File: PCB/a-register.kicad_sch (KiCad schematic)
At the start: 12 parts

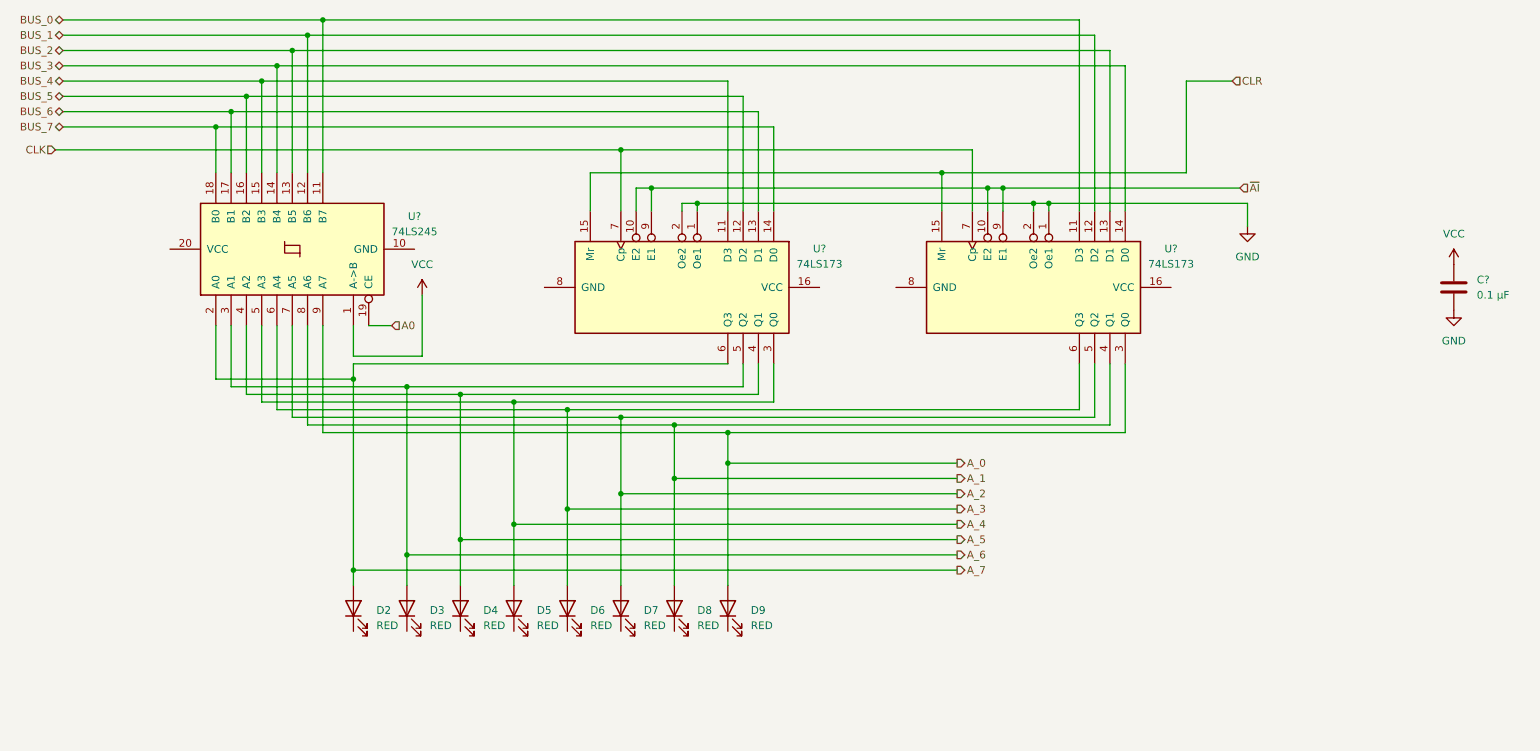
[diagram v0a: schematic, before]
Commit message: Cleaned up the schematic and got started on assigning all the footprints to the symbols
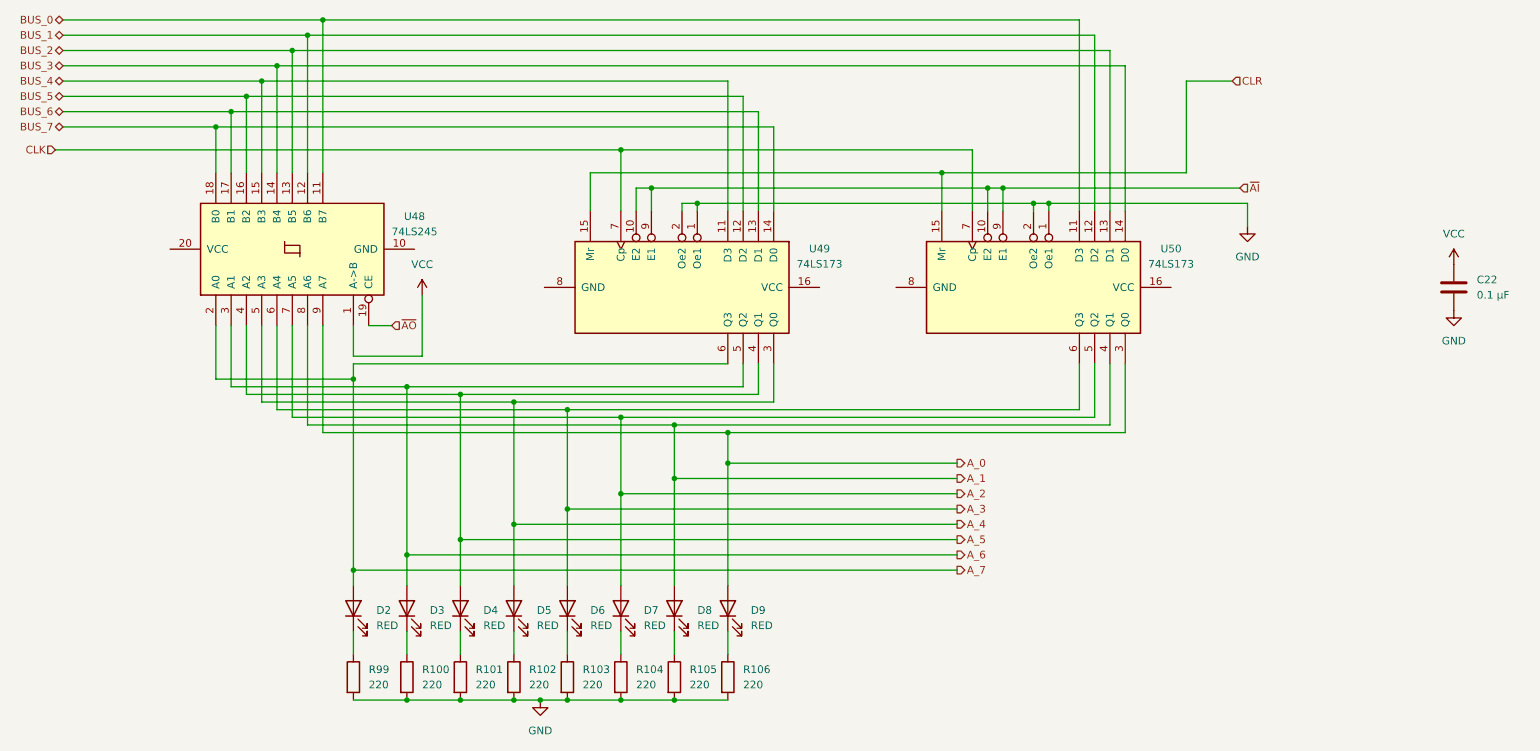
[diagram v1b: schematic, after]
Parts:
- added R100, R101, R102, R103, R104, R105, R106, R99: 220, Resistor_THT:R_Axial_DIN0207_L6.3mm_D2.5mm_P7.62mm_Horizontal, symbol Device:R
- C22: renamed from C?; footprint (none) -> Capacitor_THT:C_Radial_D5.0mm_H5.0mm_P2.00mm
- gave numbers to parts that had none: 3
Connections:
- net GND: now also R100.2, R101.2, R102.2, R103.2, R104.2, R105.2, R106.2, R99.2
- net at D8.1 (K): now also R105.1
- net at D7.1 (K): now also R104.1
- net at D2.1 (K): now also R99.1
- net at D3.1 (K): now also R100.1
- net at D4.1 (K): now also R101.1
- net at D5.1 (K): now also R102.1
- net at D9.1 (K): now also R106.1
- net at D6.1 (K): now also R103.1
- net A0 renamed ~{AO}

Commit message: added more models to work with on my pcb
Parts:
- U48: footprint (none) -> Custom:DIP254P762X508-20
- U49, U50: footprint (none) -> Custom:SN74LS173AN
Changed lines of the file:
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@@
 			)
 		)
-		(property "Footprint" ""
+		(property "Footprint" "Custom:SN74LS173AN"
 			(at 190.5 64.77 0)
 			(effects
@@
 			)
 		)
-		(property "Footprint" ""
+		(property "Footprint" "Custom:DIP254P762X508-20"
 			(at 67.31 58.42 0)
 			(effects
@@
 			)
 		)
-		(property "Footprint" ""
+		(property "Footprint" "Custom:SN74LS173AN"
 			(at 132.08 64.77 0)
 			(effects

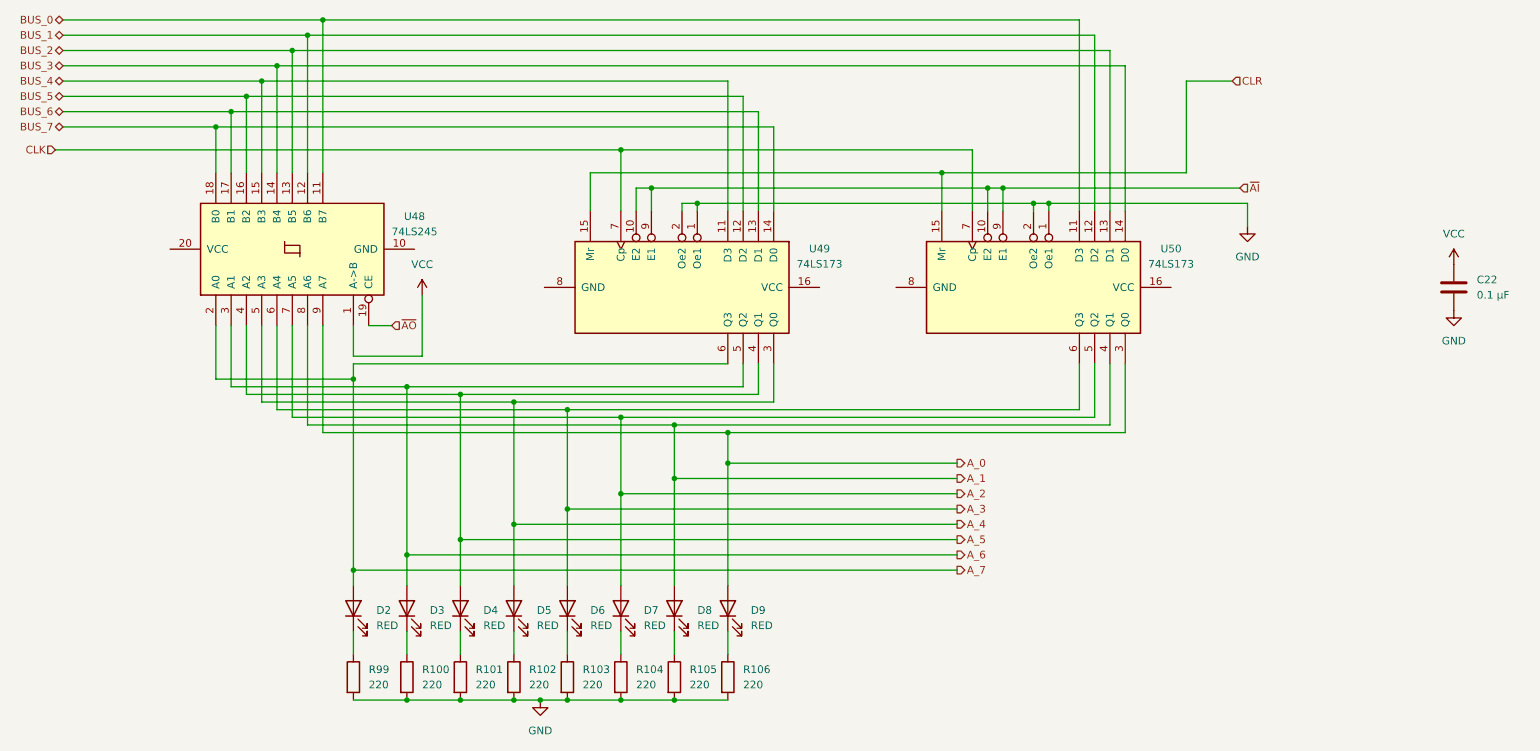
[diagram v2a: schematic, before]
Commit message: Fixed a bunch of ERC errors so know there is only one remaining.
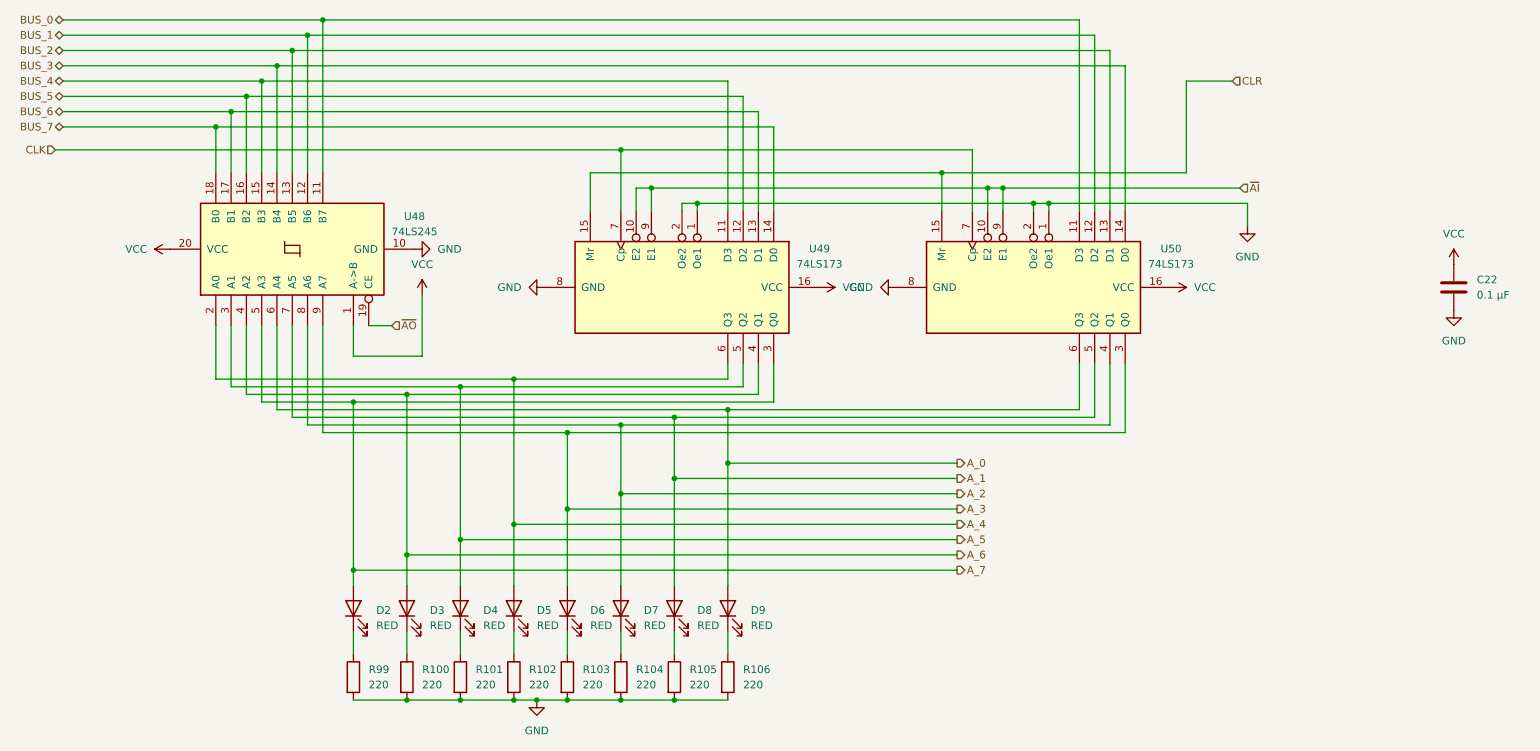
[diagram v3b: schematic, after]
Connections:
- net A_0: now also U48.6 (A4), U50.6 (Q3); no longer U48.9 (A7), U50.3 (Q0)
- net A_1: now also U48.7 (A5), U50.5 (Q2); no longer U48.8 (A6), U50.4 (Q1)
- net A_2: now also U48.8 (A6), U50.4 (Q1); no longer U48.7 (A5), U50.5 (Q2)
- net A_3: now also U48.9 (A7), U50.3 (Q0); no longer U48.6 (A4), U50.6 (Q3)
- net A_4: now also U48.2 (A0), U49.6 (Q3); no longer U48.5 (A3), U49.3 (Q0)
- net A_5: now also U48.3 (A1), U49.5 (Q2); no longer U48.4 (A2), U49.4 (Q1)
- net A_6: now also U48.4 (A2), U49.4 (Q1); no longer U48.3 (A1), U49.5 (Q2)
- net A_7: now also U48.5 (A3), U49.3 (Q0); no longer U48.2 (A0), U49.6 (Q3)
- net GND: now also U48.10 (GND), U49.8 (GND), U50.8 (GND)
- net VCC: now also U48.20 (VCC), U49.16 (VCC), U50.16 (VCC)

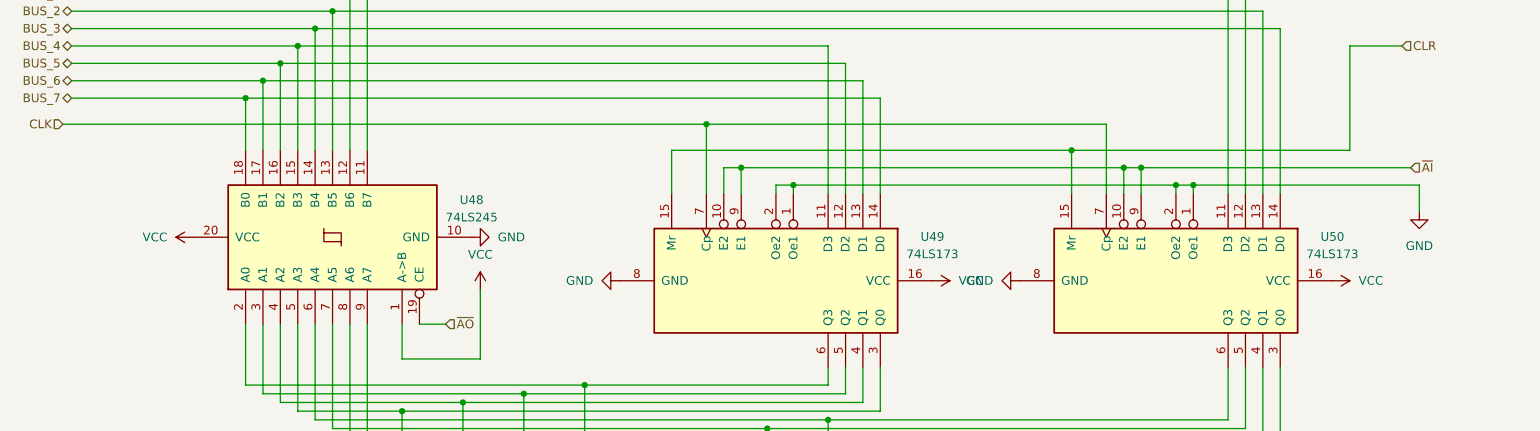
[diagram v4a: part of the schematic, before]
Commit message: Add decupling caps and reroute pcb. Updated BOM to match new number of caps
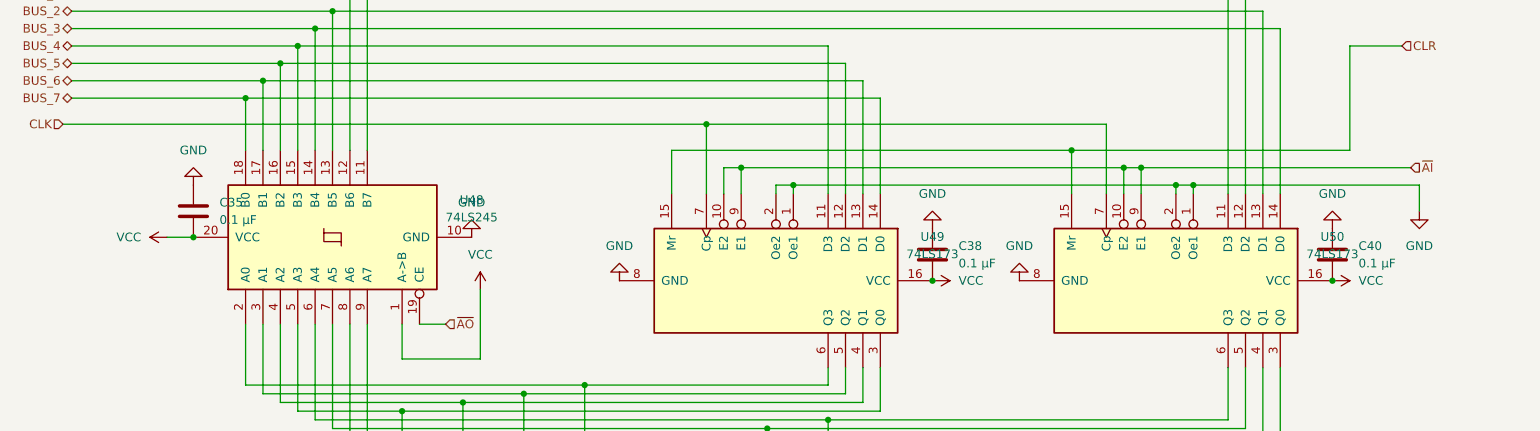
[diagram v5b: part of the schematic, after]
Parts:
- added C35, C38, C40: 0.1 µF, Capacitor_THT:C_Radial_D5.0mm_H5.0mm_P2.00mm, symbol Device:C
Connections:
- net GND: now also C35.1, C38.1, C40.1
- net VCC: now also C35.2, C38.2, C40.2
